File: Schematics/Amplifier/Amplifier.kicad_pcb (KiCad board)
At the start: 2 copper layers, 38 parts, among them J1 Conn_01x03_Female, J2 Conn_01x03_Female, J3 Conn_01x03_Female, J4 Conn_01x03_Female, Q1 BD139, Q2 BD138, Q3 BD139, Q4 BD138, U1 NE5532

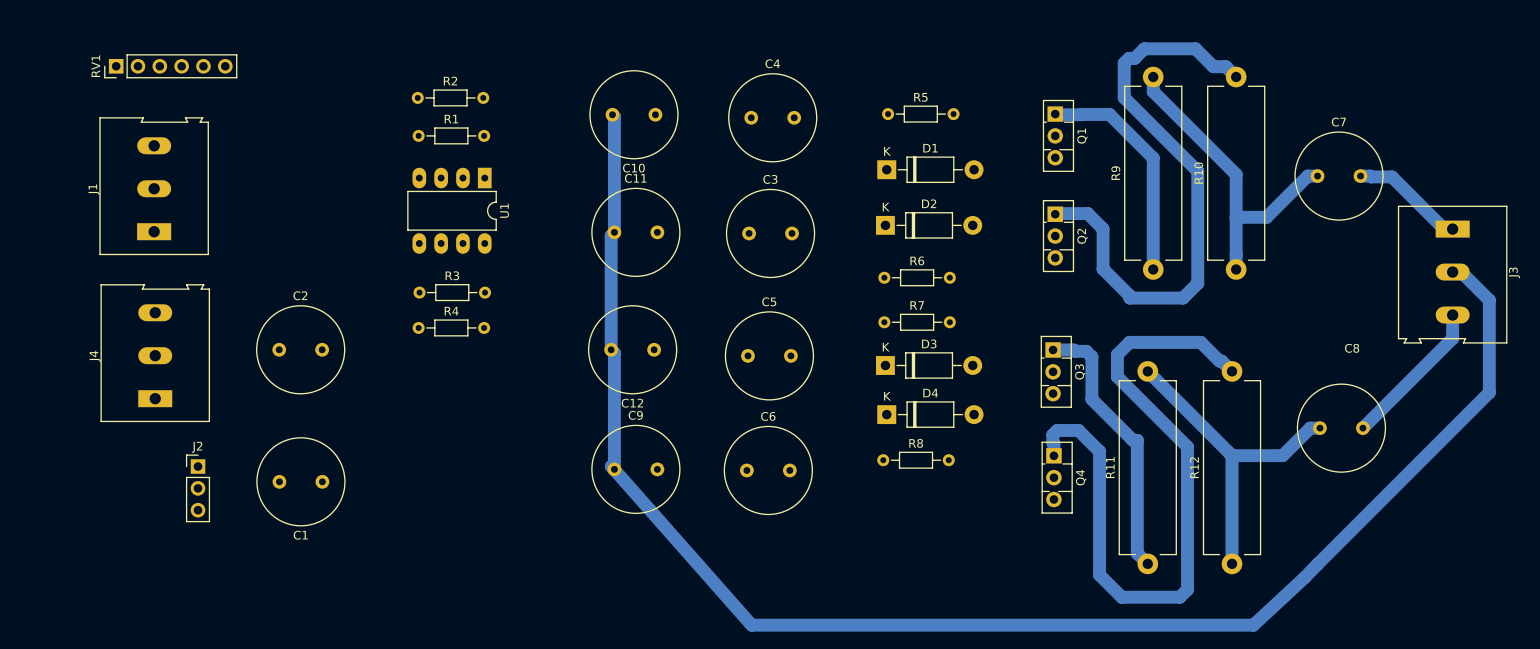
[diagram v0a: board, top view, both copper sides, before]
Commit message: Continue Amp schematic/PCB
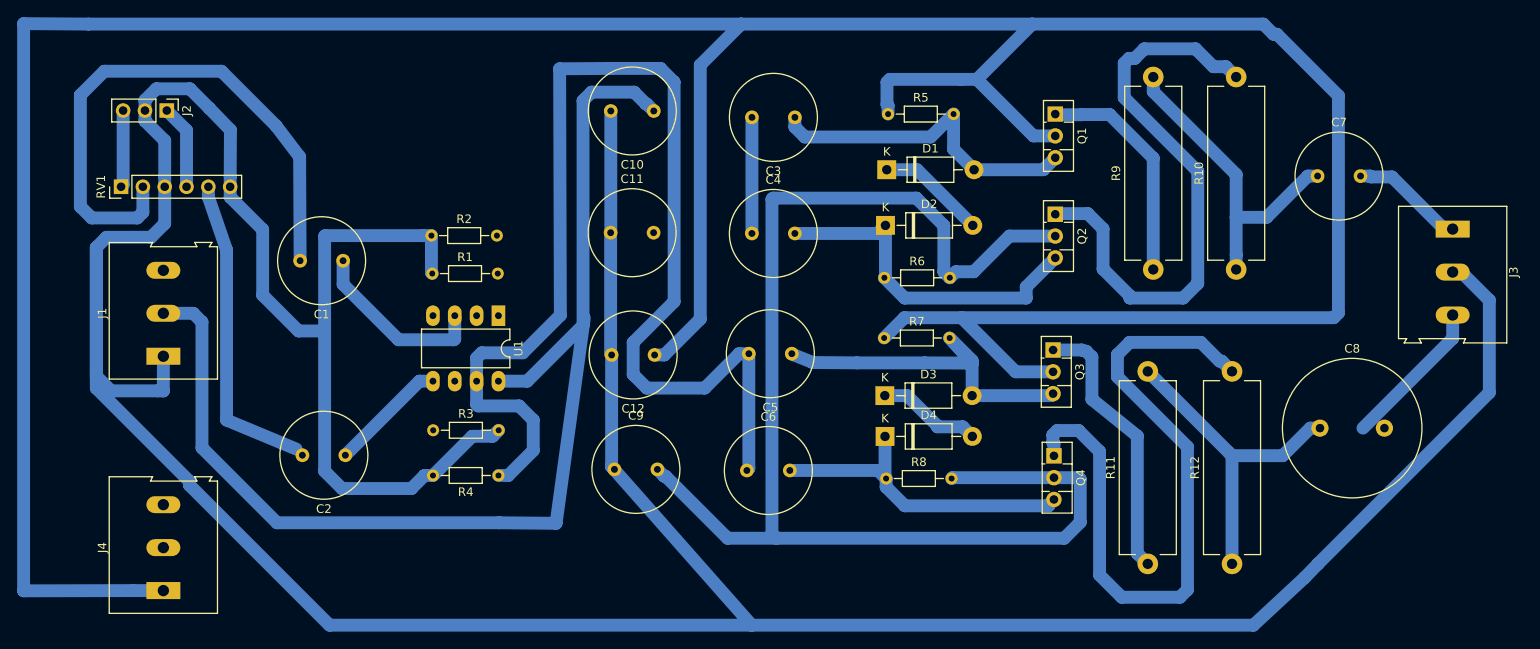
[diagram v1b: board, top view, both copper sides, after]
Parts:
- C8: footprint Capacitor_THT:C_Radial_D10.0mm_H12.5mm_P5.00mm -> Capacitor_THT:C_Radial_D16.0mm_H25.0mm_P7.50mm
- moved J2 41.6 mm to (97.7, 79.2), turned to 270 degrees
- moved C1 25.8 mm to (118.2, 96.6)
- moved J4 22.4 mm to (97.3, 135.0)
- moved R4 19.5 mm to (136.3, 121.6), turned to 180 degrees
- moved R2 16.1 mm to (128.5, 93.7)
- moved U1 16.1 mm to (136.3, 103.0)
- moved R3 16.1 mm to (128.7, 116.4)
- moved R1 16.1 mm to (128.6, 98.1)
- moved J1 14.5 mm to (97.3, 107.8)
- moved C3 14.5 mm to (170.8, 80.0), turned to 180 degrees
- moved C2 14.5 mm to (118.4, 119.3), turned to 180 degrees
- moved RV1 14.0 mm to (92.3, 88.0)
- moved C4 13.5 mm to (165.8, 93.5)
- moved C5 5.11 mm to (170.4, 107.5), turned to 180 degrees
- moved D3 3.51 mm to (181.2, 112.3)
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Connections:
- J1 pad 3: Net-(J1-Pad3) -> (no net)
- R1 pad 1: Net-(R1-Pad1) -> GND
- R1 pad 2: GND -> Net-(R1-Pad2)
- R2 pad 1: Net-(R2-Pad1) -> GND
- R2 pad 2: GND -> Net-(R2-Pad2)
- R3 pad 2: Net-(R1-Pad1) -> GND
- R4 pad 2: Net-(R2-Pad1) -> GND
- U1 pad 2: GND -> Net-(R1-Pad2)
- U1 pad 6: GND -> Net-(R2-Pad2)
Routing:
- net Net-(C12-Pad1): track 0.00 -> 410.0 mm
- net GND: track 180.2 -> 447.1 mm
- net Net-(C9-Pad2): track 0.00 -> 155.1 mm
- net Net-(C5-Pad2): track 0.00 -> 141.5 mm
- net Net-(C10-Pad1): track 0.00 -> 136.7 mm
- net Net-(C1-Pad2): track 0.00 -> 67.2 mm
- net Net-(C5-Pad1): track 0.00 -> 42.5 mm
- net Net-(C4-Pad2): track 0.00 -> 40.6 mm
- net Net-(C3-Pad1): track 0.00 -> 38.7 mm
- net Net-(C6-Pad2): track 0.00 -> 38.4 mm
- net Net-(C2-Pad2): track 0.00 -> 36.3 mm
- net Net-(C1-Pad1): track 0.00 -> 21.2 mm
- net Net-(C2-Pad1): track 0.00 -> 13.8 mm
- net Net-(C3-Pad2): track 0.00 -> 13.5 mm
- net Net-(D1-Pad1): track 0.00 -> 12.7 mm
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
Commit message: continuing PCB for amplifier
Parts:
- moved R3 7.74 mm to (136.4, 116.6), turned to 180 degrees
- moved R1 1.15 mm to (128.7, 97.0)
- moved R2 1.15 mm to (128.6, 92.6)
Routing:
- net Net-(C11-Pad2): track 0.00 -> 171.7 mm, vias 0 -> 4
- net Net-(C3-Pad2): track 13.5 -> 92.2 mm, vias 0 -> 4
- net Net-(C9-Pad2): track 155.1 -> 223.8 mm, vias 0 -> 4
- net GND: track 447.1 -> 436.6 mm
- net Net-(R1-Pad2): track 0.00 -> 7.58 mm
- net Net-(C5-Pad2): track 141.5 -> 140.3 mm
